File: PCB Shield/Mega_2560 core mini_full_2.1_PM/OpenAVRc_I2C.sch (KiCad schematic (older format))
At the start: 11 parts, among them P2 LCD_I2C, U7 FM24W256, U8 DS3231SN

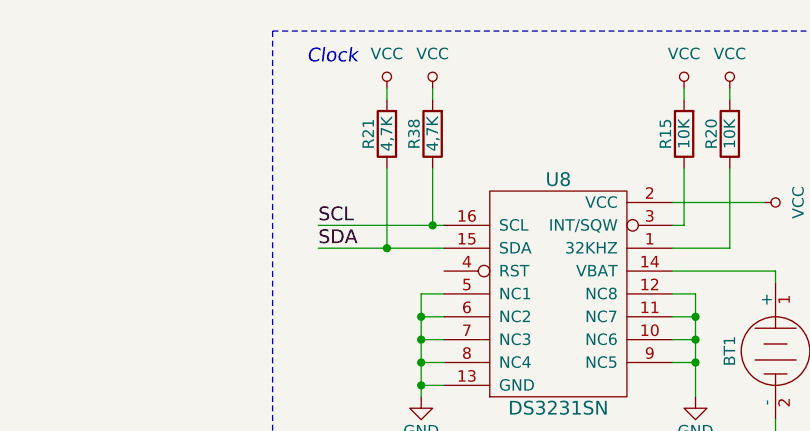
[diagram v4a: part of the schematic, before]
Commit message: Udpade shild v2.1
remove c10 on VREF and R21,R38 on I2C
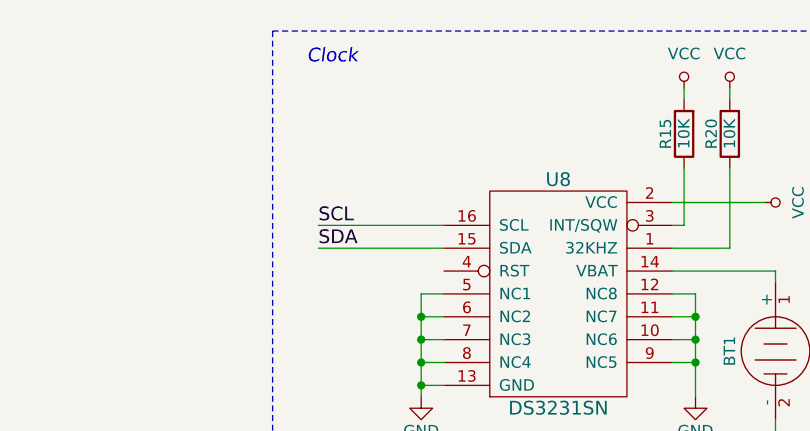
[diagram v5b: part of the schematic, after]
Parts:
- removed R21, R38: 4,7K, Resistors_SMD:R_1206, symbol R-RESCUE-Mega_2560_core_mini_full_2.0
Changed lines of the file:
@@
 Sheet 5 7
 Title "Shield Mega2560 core Full"
-Date "2018-03-16"
+Date "2018-04-19"
 Rev "2.10"
 Comp "© Team OpenAVRc"
@@
 $EndComp
 $Comp
-L GND-RESCUE-Mega_2560_core_mini_full_2.0 #PWR085
+L GND-RESCUE-Mega_2560_core_mini_full_2.0 #PWR084
 U 1 1 59C56715
 P 8250 4650
-F 0 "#PWR085" H 8250 4400 50  0001 C CNN
+F 0 "#PWR084" H 8250 4400 50  0001 C CNN
 F 1 "GND" H 8250 4500 50  0000 C CNN
 F 2 "" H 8250 4650 50  0000 C CNN
@@
 $EndComp
 $Comp
-L VCC #PWR086
+L VCC #PWR085
 U 1 1 59C5671B
 P 8250 3350
-F 0 "#PWR086" H 8250 3200 50  0001 C CNN
+F 0 "#PWR085" H 8250 3200 50  0001 C CNN
 F 1 "VCC" H 8250 3500 50  0000 C CNN
 F 2 "" H 8250 3350 50  0000 C CNN
@@
 $EndComp
 $Comp
-L GND-RESCUE-Mega_2560_core_mini_full_2.0 #PWR087
+L GND-RESCUE-Mega_2560_core_mini_full_2.0 #PWR086
 U 1 1 59C56728
 P 8700 3450
-F 0 "#PWR087" H 8700 3200 50  0001 C CNN
+F 0 "#PWR086" H 8700 3200 50  0001 C CNN
 F 1 "GND" H 8700 3300 50  0000 C CNN
 F 2 "" H 8700 3450 50  0000 C CNN
@@
 Sda
 $Comp
-L GND-RESCUE-Mega_2560_core_mini_full_2.0 #PWR088
+L GND-RESCUE-Mega_2560_core_mini_full_2.0 #PWR087
 U 1 1 59C56730
 P 9050 3950
-F 0 "#PWR088" H 9050 3700 50  0001 C CNN
+F 0 "#PWR087" H 9050 3700 50  0001 C CNN
 F 1 "GND" H 9050 3800 50  0000 C CNN
 F 2 "" H 9050 3950 50  0000 C CNN
@@
 $EndComp
 $Comp
-L GND-RESCUE-Mega_2560_core_mini_full_2.0 #PWR089
+L GND-RESCUE-Mega_2560_core_mini_full_2.0 #PWR088
 U 1 1 59C5673F
 P 4550 4600
-F 0 "#PWR089" H 4550 4350 50  0001 C CNN
+F 0 "#PWR088" H 4550 4350 50  0001 C CNN
 F 1 "GND" H 4550 4450 50  0000 C CNN
 F 2 "" H 4550 4600 50  0000 C CNN
@@
 $EndComp
 $Comp
-L GND-RESCUE-Mega_2560_core_mini_full_2.0 #PWR090
+L GND-RESCUE-Mega_2560_core_mini_full_2.0 #PWR089
 U 1 1 59C56745
 P 5750 4600
-F 0 "#PWR090" H 5750 4350 50  0001 C CNN
+F 0 "#PWR089" H 5750 4350 50  0001 C CNN
 F 1 "GND" H 5750 4450 50  0000 C CNN
 F 2 "" H 5750 4600 50  0000 C CNN
@@
 $EndComp
 $Comp
-L GND-RESCUE-Mega_2560_core_mini_full_2.0 #PWR091
+L GND-RESCUE-Mega_2560_core_mini_full_2.0 #PWR090
 U 1 1 59C5674B
 P 6100 4800
-F 0 "#PWR091" H 6100 4550 50  0001 C CNN
+F 0 "#PWR090" H 6100 4550 50  0001 C CNN
 F 1 "GND" H 6100 4650 50  0000 C CNN
 F 2 "" H 6100 4800 50  0000 C CNN
@@
 $EndComp
 $Comp
-L VCC #PWR092
+L VCC #PWR091
 U 1 1 59C56758
 P 6350 3250
-F 0 "#PWR092" H 6350 3100 50  0001 C CNN
+F 0 "#PWR091" H 6350 3100 50  0001 C CNN
 F 1 "VCC" H 6350 3400 50  0000 C CNN
 F 2 "" H 6350 3250 50  0000 C CNN
@@
 $EndComp
 $Comp
-L GND-RESCUE-Mega_2560_core_mini_full_2.0 #PWR093
+L GND-RESCUE-Mega_2560_core_mini_full_2.0 #PWR092
 U 1 1 59C5675E
 P 6350 3650
-F 0 "#PWR093" H 6350 3400 50  0001 C CNN
+F 0 "#PWR092" H 6350 3400 50  0001 C CNN
 F 1 "GND" H 6350 3500 50  0000 C CNN
 F 2 "" H 6350 3650 50  0000 C CNN
@@
 $EndComp
 $Comp
-L VCC #PWR094
+L VCC #PWR093
 U 1 1 59C56764
 P 6050 3750
-F 0 "#PWR094" H 6050 3600 50  0001 C CNN
+F 0 "#PWR093" H 6050 3600 50  0001 C CNN
 F 1 "VCC" H 6050 3900 50  0000 C CNN
 F 2 "" H 6050 3750 50  0000 C CNN
@@
 $EndComp
 $Comp
-L VCC #PWR095
+L VCC #PWR094
 U 1 1 59C56778
 P 5900 3250
-F 0 "#PWR095" H 5900 3100 50  0001 C CNN
+F 0 "#PWR094" H 5900 3100 50  0001 C CNN
 F 1 "VCC" H 5900 3400 50  0000 C CNN
 F 2 "" H 5900 3250 50  0000 C CNN
@@
 $EndComp
 $Comp
-L VCC #PWR096
+L VCC #PWR095
 U 1 1 59C5677E
 P 5700 3250
-F 0 "#PWR096" H 5700 3100 50  0001 C CNN
+F 0 "#PWR095" H 5700 3100 50  0001 C CNN
 F 1 "VCC" H 5700 3400 50  0000 C CNN
 F 2 "" H 5700 3250 50  0000 C CNN
@@
 $EndComp
 $Comp
-L GND-RESCUE-Mega_2560_core_mini_full_2.0 #PWR097
+L GND-RESCUE-Mega_2560_core_mini_full_2.0 #PWR096
 U 1 1 59C56784
 P 7450 4150
-F 0 "#PWR097" H 7450 3900 50  0001 C CNN
+F 0 "#PWR096" H 7450 3900 50  0001 C CNN
 F 1 "GND" H 7450 4000 50  0000 C CNN
 F 2 "" H 7450 4150 50  0000 C CNN
@@
 	7050 5000 7050 3000
 $Comp
-L VCC #PWR098
+L VCC #PWR097
 U 1 1 59C57848
 P 2250 3800
-F 0 "#PWR098" H 2250 3650 50  0001 C CNN
+F 0 "#PWR097" H 2250 3650 50  0001 C CNN
 F 1 "VCC" H 2250 3950 50  0000 C CNN
 F 2 "" H 2250 3800 50  0000 C CNN
@@
 $EndComp
 $Comp
-L GND-RESCUE-Mega_2560_core_mini_full_2.0 #PWR099
+L GND-RESCUE-Mega_2560_core_mini_full_2.0 #PWR098
 U 1 1 59C5784E
 P 2550 3800
-F 0 "#PWR099" H 2550 3550 50  0001 C CNN
+F 0 "#PWR098" H 2550 3550 50  0001 C CNN
 F 1 "GND" H 2550 3650 50  0000 C CNN
 F 2 "" H 2550 3800 50  0000 C CNN
@@
 Text GLabel 1750 3550 0    60   BiDi ~ 0
 Sda
-$Comp
-L R-RESCUE-Mega_2560_core_mini_full_2.0 R21
-U 1 1 59D4D3D2
-P 4400 3450
-F 0 "R21" V 4480 3450 50  0000 C CNN
-F 1 "4,7K" V 4400 3450 50  0000 C CNN
-F 2 "Resistors_SMD:R_1206" V 4330 3450 50  0001 C CNN
-F 3 "" H 4400 3450 50  0000 C CNN
-	1    4400 3450
-	-1   0    0    1
-$EndComp
-$Comp
-L R-RESCUE-Mega_2560_core_mini_full_2.0 R38
-U 1 1 59D4D3D8
-P 4600 3450
-F 0 "R38" V 4680 3450 50  0000 C CNN
-F 1 "4,7K" V 4600 3450 50  0000 C CNN
-F 2 "Resistors_SMD:R_1206" V 4530 3450 50  0001 C CNN
-F 3 "" H 4600 3450 50  0000 C CNN
-	1    4600 3450
-	-1   0    0    1
-$EndComp
-$Comp
-L VCC #PWR0100
-U 1 1 59D4D3DE
-P 4600 3250
-F 0 "#PWR0100" H 4600 3100 50  0001 C CNN
-F 1 "VCC" H 4600 3400 50  0000 C CNN
-F 2 "" H 4600 3250 50  0000 C CNN
-F 3 "" H 4600 3250 50  0000 C CNN
-	1    4600 3250
-	1    0    0    -1
-$EndComp
-$Comp
-L VCC #PWR0101
-U 1 1 59D4D3E4
-P 4400 3250
-F 0 "#PWR0101" H 4400 3100 50  0001 C CNN
-F 1 "VCC" H 4400 3400 50  0000 C CNN
-F 2 "" H 4400 3250 50  0000 C CNN
-F 3 "" H 4400 3250 50  0000 C CNN
-	1    4400 3250
-	1    0    0    -1
-$EndComp
-Wire Wire Line
-	4400 3300 4400 3250
-Wire Wire Line
-	4600 3300 4600 3250
-Wire Wire Line
-	4600 3600 4600 3850
-Connection ~ 4600 3850
-Wire Wire Line
-	4400 3600 4400 3950
-Connection ~ 4400 3950
 Text Notes 2000 3050 0    60   ~ 0
 (Option)

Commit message: Update pcb shield
Update core component (change pin 99 from GND to AGND).
Remove GND on AGND pin.
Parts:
- U7: footprint SOIC-8-FRAM_DI -> v2.1:SOIC-8-FRAM_DI
- U8: footprint SO-16-DS3231 -> v2.1:SO-16-DS3231
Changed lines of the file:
@@
 Sheet 5 7
 Title "Shield Mega2560 core Full"
-Date "2018-04-19"
+Date "2018-04-25"
 Rev "2.10"
 Comp "© Team OpenAVRc"
@@
 F 0 "U7" H 8400 4400 60  0000 C CNN
 F 1 "FM24W256" H 8500 3700 60  0000 C CNN
-F 2 "SOIC-8-FRAM_DI" H 8250 4050 60  0001 C CNN
+F 2 "v2.1:SOIC-8-FRAM_DI" H 8250 4050 60  0001 C CNN
 F 3 "" H 8250 4050 60  0001 C CNN
 	1    8250 4050
@@
 $EndComp
 $Comp
-L GND-RESCUE-Mega_2560_core_mini_full_2.0 #PWR084
+L GND-RESCUE-Mega_2560_core_mini_full_2.0 #PWR085
 U 1 1 59C56715
 P 8250 4650
-F 0 "#PWR084" H 8250 4400 50  0001 C CNN
+F 0 "#PWR085" H 8250 4400 50  0001 C CNN
 F 1 "GND" H 8250 4500 50  0000 C CNN
 F 2 "" H 8250 4650 50  0000 C CNN
@@
 $EndComp
 $Comp
-L VCC #PWR085
+L VCC #PWR086
 U 1 1 59C5671B
 P 8250 3350
-F 0 "#PWR085" H 8250 3200 50  0001 C CNN
+F 0 "#PWR086" H 8250 3200 50  0001 C CNN
 F 1 "VCC" H 8250 3500 50  0000 C CNN
 F 2 "" H 8250 3350 50  0000 C CNN
@@
 $EndComp
 $Comp
-L GND-RESCUE-Mega_2560_core_mini_full_2.0 #PWR086
+L GND-RESCUE-Mega_2560_core_mini_full_2.0 #PWR087
 U 1 1 59C56728
 P 8700 3450
-F 0 "#PWR086" H 8700 3200 50  0001 C CNN
+F 0 "#PWR087" H 8700 3200 50  0001 C CNN
 F 1 "GND" H 8700 3300 50  0000 C CNN
 F 2 "" H 8700 3450 50  0000 C CNN
@@
 Sda
 $Comp
-L GND-RESCUE-Mega_2560_core_mini_full_2.0 #PWR087
+L GND-RESCUE-Mega_2560_core_mini_full_2.0 #PWR088
 U 1 1 59C56730
 P 9050 3950
-F 0 "#PWR087" H 9050 3700 50  0001 C CNN
+F 0 "#PWR088" H 9050 3700 50  0001 C CNN
 F 1 "GND" H 9050 3800 50  0000 C CNN
 F 2 "" H 9050 3950 50  0000 C CNN
@@
 F 0 "U8" H 5150 4650 60  0000 C CNN
 F 1 "DS3231SN" H 5150 3650 60  0000 C CNN
-F 2 "SO-16-DS3231" H 5100 4100 60  0001 C CNN
+F 2 "v2.1:SO-16-DS3231" H 5100 4100 60  0001 C CNN
 F 3 "" H 5100 4100 60  0001 C CNN
 	1    5150 4150
@@
 $EndComp
 $Comp
-L GND-RESCUE-Mega_2560_core_mini_full_2.0 #PWR088
+L GND-RESCUE-Mega_2560_core_mini_full_2.0 #PWR089
 U 1 1 59C5673F
 P 4550 4600
-F 0 "#PWR088" H 4550 4350 50  0001 C CNN
+F 0 "#PWR089" H 4550 4350 50  0001 C CNN
 F 1 "GND" H 4550 4450 50  0000 C CNN
 F 2 "" H 4550 4600 50  0000 C CNN
@@
 $EndComp
 $Comp
-L GND-RESCUE-Mega_2560_core_mini_full_2.0 #PWR089
+L GND-RESCUE-Mega_2560_core_mini_full_2.0 #PWR090
 U 1 1 59C56745
 P 5750 4600
-F 0 "#PWR089" H 5750 4350 50  0001 C CNN
+F 0 "#PWR090" H 5750 4350 50  0001 C CNN
 F 1 "GND" H 5750 4450 50  0000 C CNN
 F 2 "" H 5750 4600 50  0000 C CNN
@@
 $EndComp
 $Comp
-L GND-RESCUE-Mega_2560_core_mini_full_2.0 #PWR090
+L GND-RESCUE-Mega_2560_core_mini_full_2.0 #PWR091
 U 1 1 59C5674B
 P 6100 4800
-F 0 "#PWR090" H 6100 4550 50  0001 C CNN
+F 0 "#PWR091" H 6100 4550 50  0001 C CNN
 F 1 "GND" H 6100 4650 50  0000 C CNN
 F 2 "" H 6100 4800 50  0000 C CNN
@@
 $EndComp
 $Comp
-L VCC #PWR091
+L VCC #PWR092
 U 1 1 59C56758
 P 6350 3250
-F 0 "#PWR091" H 6350 3100 50  0001 C CNN
+F 0 "#PWR092" H 6350 3100 50  0001 C CNN
 F 1 "VCC" H 6350 3400 50  0000 C CNN
 F 2 "" H 6350 3250 50  0000 C CNN
@@
 $EndComp
 $Comp
-L GND-RESCUE-Mega_2560_core_mini_full_2.0 #PWR092
+L GND-RESCUE-Mega_2560_core_mini_full_2.0 #PWR093
 U 1 1 59C5675E
 P 6350 3650
-F 0 "#PWR092" H 6350 3400 50  0001 C CNN
+F 0 "#PWR093" H 6350 3400 50  0001 C CNN
 F 1 "GND" H 6350 3500 50  0000 C CNN
 F 2 "" H 6350 3650 50  0000 C CNN
@@
 $EndComp
 $Comp
-L VCC #PWR093
+L VCC #PWR094
 U 1 1 59C56764
 P 6050 3750
-F 0 "#PWR093" H 6050 3600 50  0001 C CNN
+F 0 "#PWR094" H 6050 3600 50  0001 C CNN
 F 1 "VCC" H 6050 3900 50  0000 C CNN
 F 2 "" H 6050 3750 50  0000 C CNN
@@
 $EndComp
 $Comp
-L VCC #PWR094
+L VCC #PWR095
 U 1 1 59C56778
 P 5900 3250
-F 0 "#PWR094" H 5900 3100 50  0001 C CNN
+F 0 "#PWR095" H 5900 3100 50  0001 C CNN
 F 1 "VCC" H 5900 3400 50  0000 C CNN
 F 2 "" H 5900 3250 50  0000 C CNN
@@
 $EndComp
 $Comp
-L VCC #PWR095
+L VCC #PWR096
 U 1 1 59C5677E
 P 5700 3250
-F 0 "#PWR095" H 5700 3100 50  0001 C CNN
+F 0 "#PWR096" H 5700 3100 50  0001 C CNN
 F 1 "VCC" H 5700 3400 50  0000 C CNN
 F 2 "" H 5700 3250 50  0000 C CNN
@@
 $EndComp
 $Comp
-L GND-RESCUE-Mega_2560_core_mini_full_2.0 #PWR096
+L GND-RESCUE-Mega_2560_core_mini_full_2.0 #PWR097
 U 1 1 59C56784
 P 7450 4150
-F 0 "#PWR096" H 7450 3900 50  0001 C CNN
+F 0 "#PWR097" H 7450 3900 50  0001 C CNN
 F 1 "GND" H 7450 4000 50  0000 C CNN
 F 2 "" H 7450 4150 50  0000 C CNN
@@
 	7050 5000 7050 3000
 $Comp
-L VCC #PWR097
+L VCC #PWR098
 U 1 1 59C57848
 P 2250 3800
-F 0 "#PWR097" H 2250 3650 50  0001 C CNN
+F 0 "#PWR098" H 2250 3650 50  0001 C CNN
 F 1 "VCC" H 2250 3950 50  0000 C CNN
 F 2 "" H 2250 3800 50  0000 C CNN
@@
 $EndComp
 $Comp
-L GND-RESCUE-Mega_2560_core_mini_full_2.0 #PWR098
+L GND-RESCUE-Mega_2560_core_mini_full_2.0 #PWR099
 U 1 1 59C5784E
 P 2550 3800
-F 0 "#PWR098" H 2550 3550 50  0001 C CNN
+F 0 "#PWR099" H 2550 3550 50  0001 C CNN
 F 1 "GND" H 2550 3650 50  0000 C CNN
 F 2 "" H 2550 3800 50  0000 C CNN
